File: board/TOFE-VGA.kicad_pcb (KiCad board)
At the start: 4 copper layers, 46 x 3 mm, 114 parts, among them P1 CONN_02X06, P601 3-RCA, U5V1 LP2985

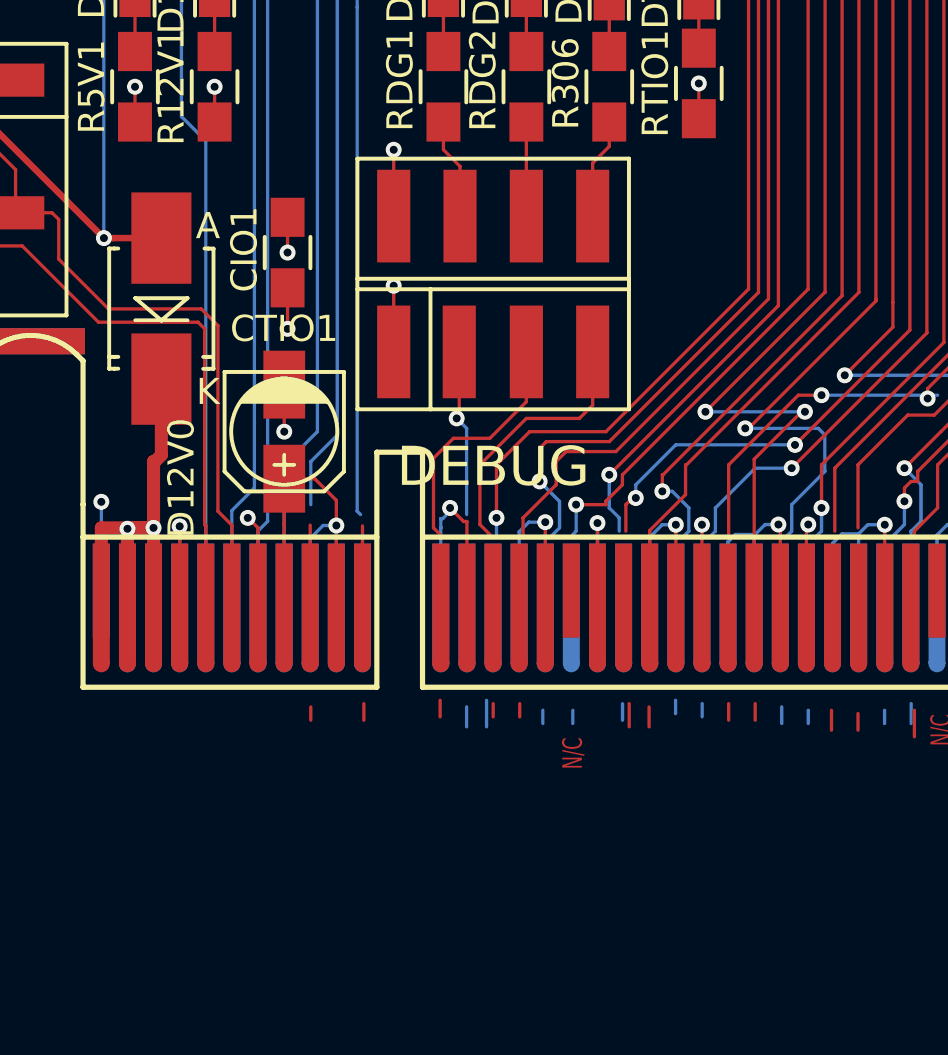
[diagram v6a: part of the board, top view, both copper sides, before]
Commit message: Updating PCB.
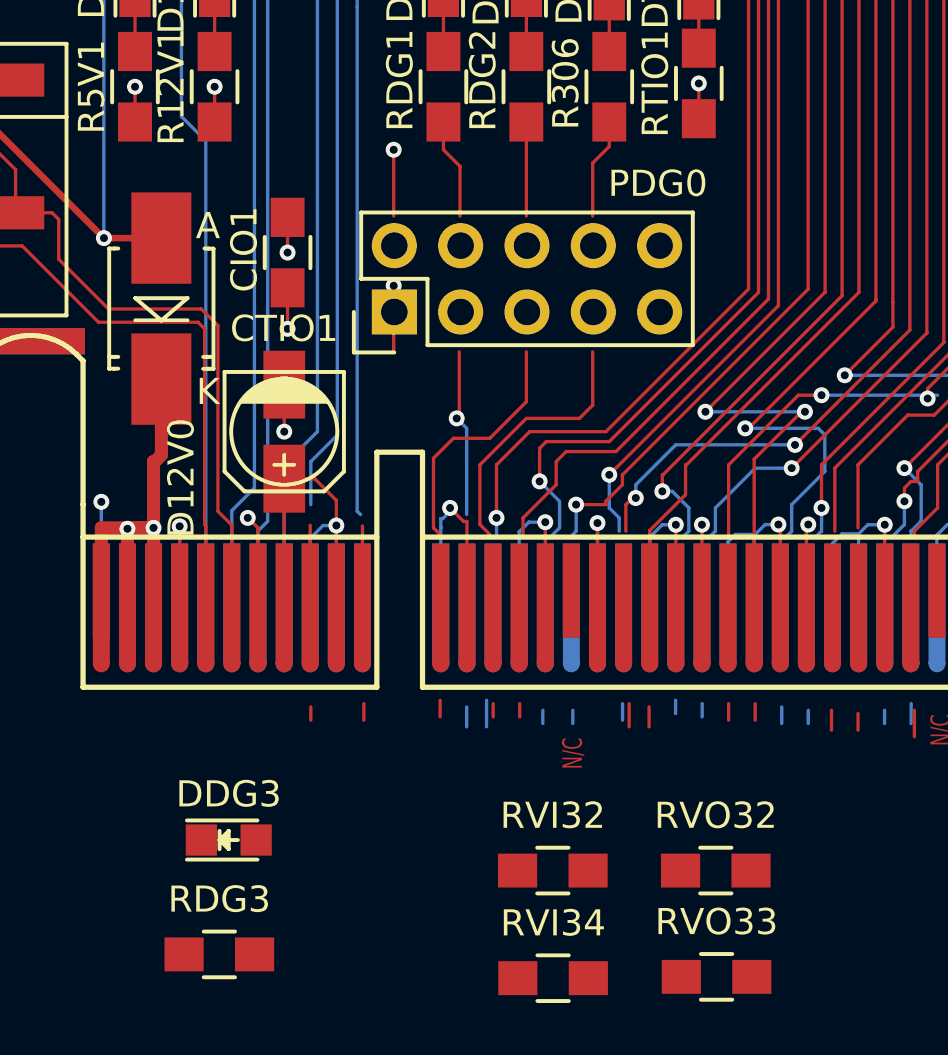
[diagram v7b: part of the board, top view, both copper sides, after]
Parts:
- added DDG3: LED, LEDs:LED_0805, F.Cu at (112.8, 164.3)
- added RDG3: 68R, Resistors_SMD:R_0805_HandSoldering, F.Cu at (112.4, 168.7)
- added RVI32: ?, Resistors_SMD:R_0805_HandSoldering, F.Cu at (125.2, 165.5)
- added RVI34: ?, Resistors_SMD:R_0805_HandSoldering, F.Cu at (125.2, 169.6)
- added RVO32: ?, Resistors_SMD:R_0805_HandSoldering, F.Cu at (131.4, 165.5)
- added RVO33: ?, Resistors_SMD:R_0805_HandSoldering, F.Cu at (131.5, 169.6)
- PDG0: footprint CON-SMD-2.54:TE-AMPMODU-MOD-II-4X2 -> Pin_Headers:Pin_Header_Straight_2x05
- moved PDG0 3.93 mm to (119.1, 144.1), turned to 90 degrees
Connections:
- PDG0 pad 3: Net-(PDG0-Pad3) -> /TOFE-VGA/TOFE/VGAIN_I2C_EN
- PDG0 pad 5: Net-(PDG0-Pad5) -> /TOFE-VGA/TOFE/VGAOUT_I2C_EN
- PDG0 pad 8: GND -> Net-(PDG0-Pad8)
- TOFE0 pad A13: Net-(PDG0-Pad3) -> /TOFE-VGA/TOFE/VGAIN_I2C_EN
- TOFE0 pad A14: Net-(PDG0-Pad5) -> /TOFE-VGA/TOFE/VGAOUT_I2C_EN
- TOFE0 pad A16: /TOFE-VGA/AD9984/FIELD -> Net-(PDG0-Pad7)
- TOFE0 pad A17: /TOFE-VGA/TOFE/VGAOUT_I2C_EN -> /TOFE-VGA/AD9984/FIELD
- TOFE0 pad A19: /TOFE-VGA/TOFE/VGAIN_I2C_EN -> /TOFE-VGA/AD9984/B5
- TOFE0 pad A33: /TOFE-VGA/AD9984/B5 -> Net-(TOFE0-PadA33)
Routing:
- net Net-(PDG0-Pad8): track 0.00 -> 60.8 mm, vias 0 -> 1
- net /TOFE-VGA/AD9984/VSOUT: track 41.4 -> 5.57 mm, vias 1 -> 0
- net /TOFE-VGA/AD9984/HSOUT: track 38.0 -> 7.00 mm, vias 1 -> 0
- net /TOFE-VGA/AD9984/SOGOUT: track 37.4 -> 7.14 mm
- net Net-(PDG0-Pad7): track 10.1 -> 40.2 mm
- net (no net): track 42.2 -> 53.7 mm, vias 1 -> 4
- net Net-(PDG0-Pad5): track 9.39 -> 0.00 mm
- net /TOFE-VGA/TOFE/VGAOUT_I2C_EN: track 97.5 -> 106.9 mm
- net Net-(PDG0-Pad3): track 6.43 -> 0.00 mm, vias 1 -> 0
- net Net-(PDG0-Pad6): track 3.60 -> 8.27 mm
- net Net-(P303-Pad8): track 0.94 -> 3.87 mm
- net +3V3: track 82.5 -> 79.9 mm, vias 26 -> 25
- net Net-(PDG0-Pad1): track 2.53 -> 0.00 mm, vias 1 -> 0
- net /TOFE-VGA/AD9984/R9: track 36.4 -> 35.2 mm
- net GND: track 179.1 -> 177.9 mm
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
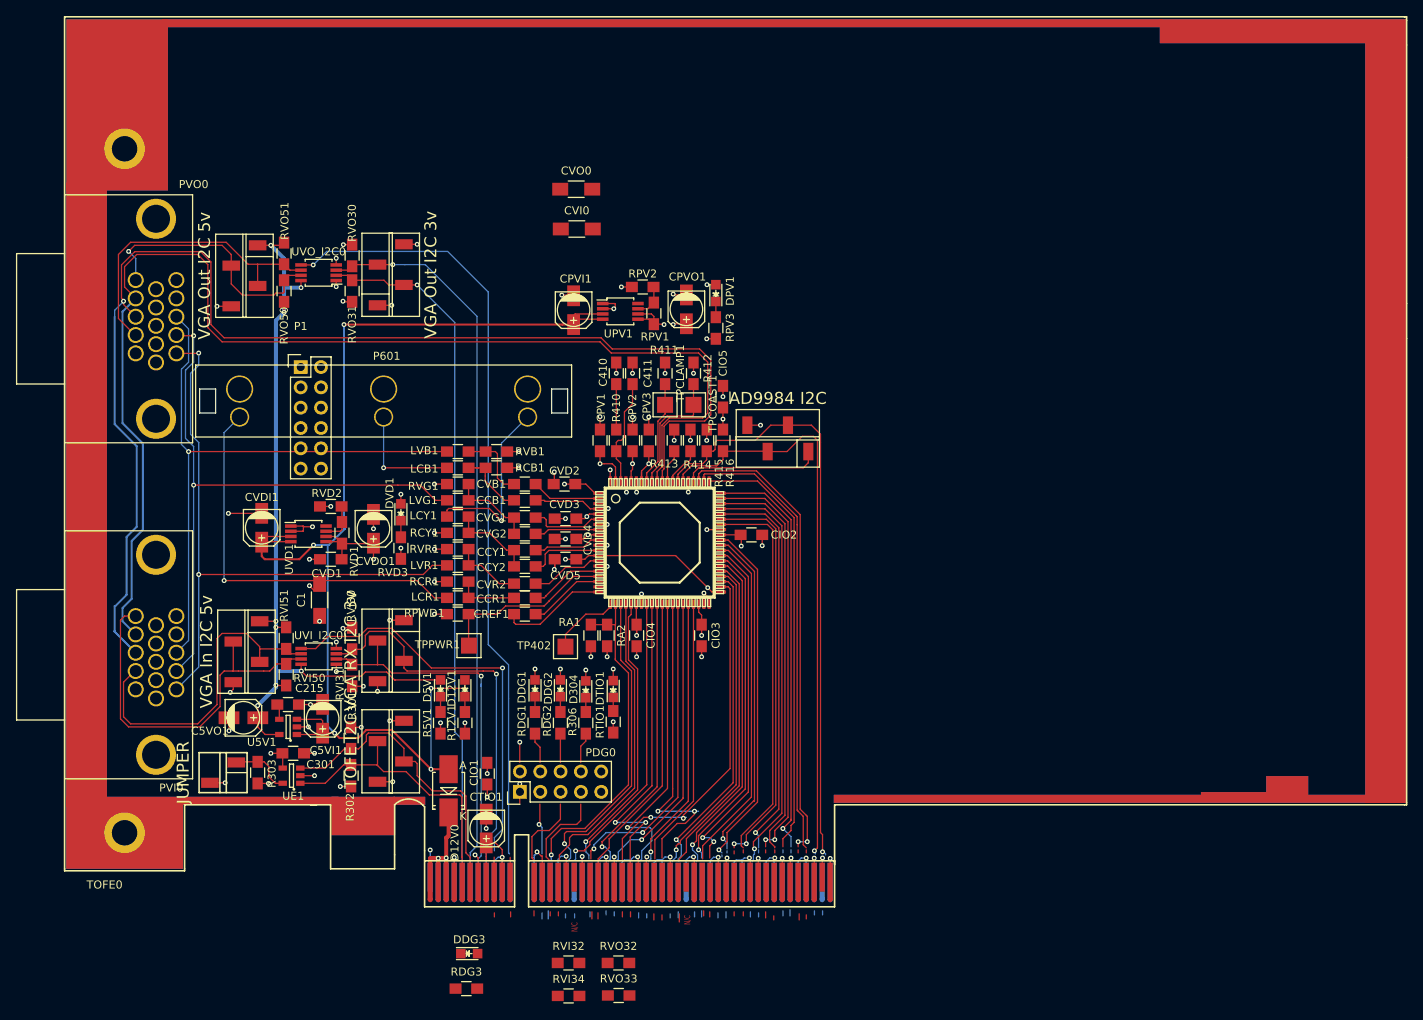
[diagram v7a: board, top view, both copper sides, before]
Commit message: Trying to import new netlist.
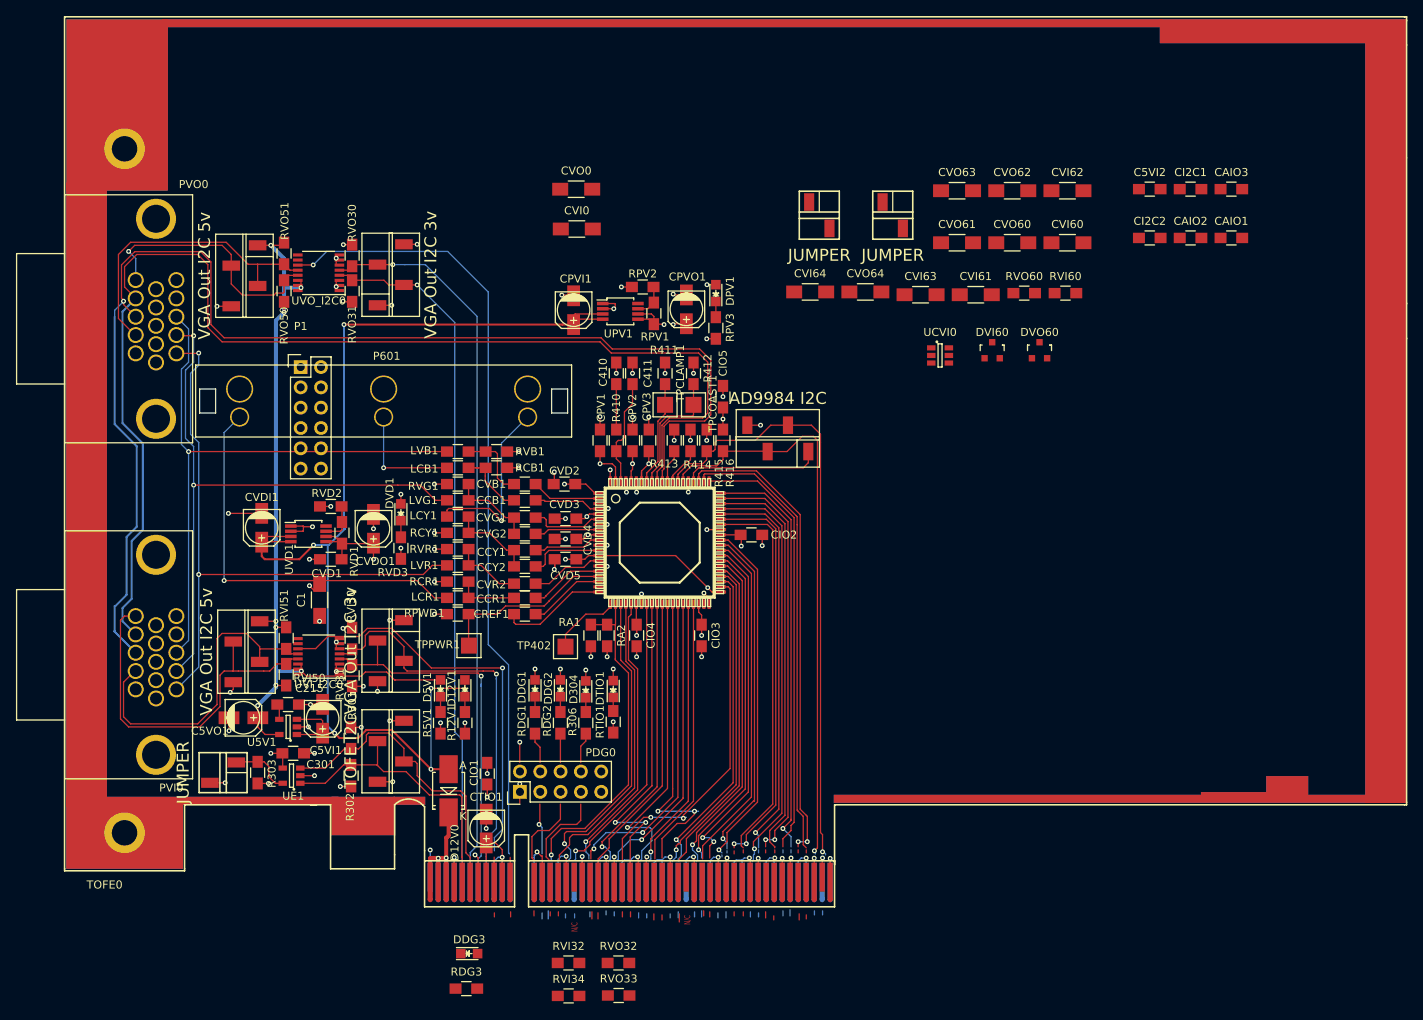
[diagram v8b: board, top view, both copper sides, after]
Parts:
- added C5VI2: 10n, Resistors_SMD:R_0805_HandSoldering, F.Cu at (197.8, 68.8)
- added CAIO1: 100n, Resistors_SMD:R_0805_HandSoldering, F.Cu at (208.0, 74.9)
- added CAIO2: 100n, Resistors_SMD:R_0805_HandSoldering, F.Cu at (202.9, 74.9)
- added CAIO3: 100n, Resistors_SMD:R_0805_HandSoldering, F.Cu at (208.0, 68.8)
- added CI2C1: 100n, Resistors_SMD:R_0805_HandSoldering, F.Cu at (202.9, 68.8)
- added CI2C2: 100n, Resistors_SMD:R_0805_HandSoldering, F.Cu at (197.8, 74.9)
- added CVI60: 100nF, Capacitors_SMD:C_1206_HandSoldering, F.Cu at (187.6, 75.5)
- added CVI61: 100nF, Capacitors_SMD:C_1206_HandSoldering, F.Cu at (176.1, 82.0)
- added CVI62: 100nF, Capacitors_SMD:C_1206_HandSoldering, F.Cu at (187.6, 69.0)
- added CVI63: 100nF, Capacitors_SMD:C_1206_HandSoldering, F.Cu at (169.2, 82.0)
- added CVI64: 100nF, Capacitors_SMD:C_1206_HandSoldering, F.Cu at (155.4, 81.6)
- added CVO60: 100nF, Capacitors_SMD:C_1206_HandSoldering, F.Cu at (180.7, 75.5)
- added CVO61: 100nF, Capacitors_SMD:C_1206_HandSoldering, F.Cu at (173.8, 75.5)
- added CVO62: 100nF, Capacitors_SMD:C_1206_HandSoldering, F.Cu at (180.7, 69.0)
- added CVO63: 100nF, Capacitors_SMD:C_1206_HandSoldering, F.Cu at (173.8, 69.0)
- added CVO64: 100nF, Capacitors_SMD:C_1206_HandSoldering, F.Cu at (162.3, 81.6)
- added DVI60: BAT54C, TO_SOT_Packages_SMD:SOT-23, F.Cu at (178.1, 88.9)
- added DVO60: BAT54C, TO_SOT_Packages_SMD:SOT-23, F.Cu at (184.1, 88.9)
- added JVI60: JUMPER, CON-SMD-2.54:HARWIN-M20-87-2x1, F.Cu at (165.7, 72.1)
- added JVO60: JUMPER, CON-SMD-2.54:HARWIN-M20-87-2x1, F.Cu at (156.5, 72.1)
- added RVI60: 2K2, Resistors_SMD:R_0805_HandSoldering, F.Cu at (187.3, 81.8)
- added RVO60: 2K2, Resistors_SMD:R_0805_HandSoldering, F.Cu at (182.2, 81.8)
- added UCVI0: SP724AH, TO_SOT_Packages_SMD:SOT-23-6, F.Cu at (171.6, 89.6)
- C5VO1: value 2u2 -> 22u
- PVI_I2C3: value VGA RX I2C 3v -> VGA Out I2C 3v
- PVI_I2C5: value VGA In I2C 5v -> VGA Out I2C 5v
- UVI_I2C0, UVO_I2C0: value TCA9617A -> TPD7S019; footprint Housings_SSOP:MSOP-8_3x3mm_Pitch0.65mm -> Housings_SSOP:SSOP-16_3.9x4.9mm_Pitch0.635mm
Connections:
- P1 pad 10: /TOFE-VGA/VGA/VGAOUT_B -> /TOFE-VGA/VGA/VGAIN_B
- P1 pad 6: /TOFE-VGA/VGA/VGAOUT_R -> /TOFE-VGA/VGA/VGAIN_R
- P1 pad 8: /TOFE-VGA/VGA/VGAOUT_G -> /TOFE-VGA/VGA/VGAIN_G
- PVI0 pad 12: /TOFE-VGA/VGA/VGAIN5V_SDA -> /TOFE-VGA/VGA/VGAOUT5V_SDA
- PVI0 pad 13: /TOFE-VGA/VGA/VGAIN_HSYNC -> /TOFE-VGA/VGA/VGAOUT_HSYNC
- PVI0 pad 14: /TOFE-VGA/VGA/VGAIN_VSYNC -> /TOFE-VGA/VGA/VGAOUT_VSYNC
- PVI0 pad 15: /TOFE-VGA/VGA/VGAIN5V_SCL -> /TOFE-VGA/VGA/VGAOUT5V_SCL
- PVI_I2C5 pad 2: /TOFE-VGA/VGA/VGAIN5V_SCL -> /TOFE-VGA/VGA/VGAOUT5V_SCL
- PVI_I2C5 pad 3: /TOFE-VGA/VGA/VGAIN5V_SDA -> /TOFE-VGA/VGA/VGAOUT5V_SDA
- PVO0 pad 1: /TOFE-VGA/VGA/VGAOUT_R -> /TOFE-VGA/VGA/VGAIN_R
- PVO0 pad 2: /TOFE-VGA/VGA/VGAOUT_G -> /TOFE-VGA/VGA/VGAIN_G
- PVO0 pad 3: /TOFE-VGA/VGA/VGAOUT_B -> /TOFE-VGA/VGA/VGAIN_B
- RVI50 pad 2: /TOFE-VGA/VGA/VGAIN5V_SCL -> /TOFE-VGA/VGA/VGAOUT5V_SCL
- RVI51 pad 2: /TOFE-VGA/VGA/VGAIN5V_SDA -> /TOFE-VGA/VGA/VGAOUT5V_SDA
- TOFE0 pad A13: /TOFE-VGA/TOFE/VGAIN_I2C_EN -> /TOFE-VGA/AD9984/VSOUT
- TOFE0 pad A14: /TOFE-VGA/TOFE/VGAOUT_I2C_EN -> /TOFE-VGA/AD9984/HSOUT
- TOFE0 pad A16: Net-(PDG0-Pad7) -> /TOFE-VGA/AD9984/R8
- TOFE0 pad A17: /TOFE-VGA/AD9984/FIELD -> /TOFE-VGA/AD9984/R7
- TOFE0 pad A19: /TOFE-VGA/AD9984/B5 -> /TOFE-VGA/AD9984/R6
- TOFE0 pad A21: /TOFE-VGA/AD9984/SDA_AD9984 -> /TOFE-VGA/AD9984/R3
- TOFE0 pad A22: /TOFE-VGA/AD9984/SCL_AD9984 -> /TOFE-VGA/AD9984/R2
- TOFE0 pad A25: /TOFE-VGA/AD9984/B0 -> /TOFE-VGA/AD9984/G9
- TOFE0 pad A26: /TOFE-VGA/AD9984/B1 -> /TOFE-VGA/AD9984/G8
- TOFE0 pad A29: /TOFE-VGA/AD9984/B2 -> /TOFE-VGA/AD9984/DATACK
- TOFE0 pad A30: /TOFE-VGA/AD9984/B3 -> /TOFE-VGA/AD9984/SOGOUT
- TOFE0 pad A32: /TOFE-VGA/AD9984/B4 -> /TOFE-VGA/AD9984/G4
- TOFE0 pad A35: /TOFE-VGA/AD9984/B6 -> /TOFE-VGA/AD9984/G1
- TOFE0 pad A36: /TOFE-VGA/AD9984/B7 -> /TOFE-VGA/AD9984/G0
- TOFE0 pad A39: /TOFE-VGA/AD9984/B8 -> /TOFE-VGA/AD9984/B7
- TOFE0 pad A40: /TOFE-VGA/AD9984/B9 -> /TOFE-VGA/AD9984/B6
- TOFE0 pad A43: /TOFE-VGA/AD9984/G0 -> /TOFE-VGA/AD9984/B3
- TOFE0 pad A44: /TOFE-VGA/AD9984/G1 -> /TOFE-VGA/AD9984/B2
- TOFE0 pad A47: /TOFE-VGA/AD9984/G2 -> /TOFE-VGA/AD9984/SDA_AD9984
- TOFE0 pad A48: /TOFE-VGA/AD9984/G3 -> /TOFE-VGA/AD9984/SCL_AD9984
- TOFE0 pad A5: /TOFE-VGA/TOFE/VGAOUT_SCL -> /TOFE-VGA/VGA/VGAOUT_SCL
- TOFE0 pad A6: /TOFE-VGA/VGA/VGAOUT_SCL -> /TOFE-VGA/TOFE/VGAOUT_SCL
- TOFE0 pad A7: /TOFE-VGA/TOFE/VGAIN_SCL -> /TOFE-VGA/VGA/VGAIN_SCL
- TOFE0 pad A8: /TOFE-VGA/VGA/VGAIN_SCL -> /TOFE-VGA/TOFE/VGAIN_SCL
- TOFE0 pad B11: /TOFE-VGA/AD9984/R1 -> /TOFE-VGA/TOFE/VGAOUT_I2C_EN
- TOFE0 pad B12: /TOFE-VGA/AD9984/R2 -> Net-(PDG0-Pad7)
- TOFE0 pad B14: /TOFE-VGA/AD9984/R3 -> /TOFE-VGA/AD9984/FIELD
- TOFE0 pad B15: /TOFE-VGA/AD9984/R4 -> /TOFE-VGA/AD9984/R9
- TOFE0 pad B20: /TOFE-VGA/AD9984/R6 -> /TOFE-VGA/AD9984/R4
- TOFE0 pad B23: /TOFE-VGA/AD9984/R7 -> /TOFE-VGA/AD9984/R1
- TOFE0 pad B24: /TOFE-VGA/AD9984/R8 -> /TOFE-VGA/AD9984/R0
- TOFE0 pad B27: /TOFE-VGA/AD9984/DATACK -> /TOFE-VGA/AD9984/G7
- TOFE0 pad B28: /TOFE-VGA/AD9984/SOGOUT -> /TOFE-VGA/AD9984/G6
- TOFE0 pad B30: /TOFE-VGA/AD9984/R9 -> /TOFE-VGA/AD9984/G5
- TOFE0 pad B33: /TOFE-VGA/AD9984/G9 -> /TOFE-VGA/AD9984/G3
- TOFE0 pad B34: /TOFE-VGA/AD9984/G8 -> /TOFE-VGA/AD9984/G2
- TOFE0 pad B37: /TOFE-VGA/AD9984/G7 -> /TOFE-VGA/AD9984/B9
- TOFE0 pad B38: /TOFE-VGA/AD9984/G6 -> /TOFE-VGA/AD9984/B8
- TOFE0 pad B41: /TOFE-VGA/AD9984/G5 -> /TOFE-VGA/AD9984/B5
- TOFE0 pad B42: /TOFE-VGA/AD9984/G4 -> /TOFE-VGA/AD9984/B4
- TOFE0 pad B45: /TOFE-VGA/AD9984/HSOUT -> /TOFE-VGA/AD9984/B1
- TOFE0 pad B46: /TOFE-VGA/AD9984/VSOUT -> /TOFE-VGA/AD9984/B0
- TOFE0 pad B9: /TOFE-VGA/AD9984/R0 -> /TOFE-VGA/TOFE/VGAIN_I2C_EN
- U5V1 pad 4: Net-(C215-Pad1) -> Net-(C5VI2-Pad1)
- UVI_I2C0 pad 1: +3V3 -> +5V
- UVI_I2C0 pad 2: /TOFE-VGA/VGA/VGAIN_SCL -> +5V
- UVI_I2C0 pad 3: /TOFE-VGA/TOFE/VGAIN_SCL -> /TOFE-VGA/VGA/VGAIN_B
- UVI_I2C0 pad 4: GND -> /TOFE-VGA/VGA/VGAIN_G
- UVI_I2C0 pad 5: /TOFE-VGA/TOFE/VGAIN_I2C_EN -> /TOFE-VGA/VGA/VGAIN_R
- UVI_I2C0 pad 6: /TOFE-VGA/VGA/VGAIN5V_SDA -> GND
- UVI_I2C0 pad 7: /TOFE-VGA/VGA/VGAIN5V_SCL -> +3V3
- UVI_I2C0 pad 8: +5V -> Net-(CVI63-Pad1)
- UVO_I2C0 pad 1: +3V3 -> +5V
- UVO_I2C0 pad 2: /TOFE-VGA/VGA/VGAOUT_SCL -> +5V
- UVO_I2C0 pad 3: /TOFE-VGA/TOFE/VGAOUT_SCL -> /TOFE-VGA/VGA/VGAIN_B
- UVO_I2C0 pad 4: GND -> /TOFE-VGA/VGA/VGAIN_G
- UVO_I2C0 pad 5: /TOFE-VGA/TOFE/VGAOUT_I2C_EN -> /TOFE-VGA/VGA/VGAIN_R
- UVO_I2C0 pad 6: /TOFE-VGA/VGA/VGAOUT5V_SDA -> GND
- UVO_I2C0 pad 7: /TOFE-VGA/VGA/VGAOUT5V_SCL -> +3V3
- UVO_I2C0 pad 8: +5V -> Net-(CVO63-Pad1)
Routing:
- net /TOFE-VGA/TOFE/VGAOUT_I2C_EN: track 106.9 -> 2.98 mm, vias 1 -> 0
- net /TOFE-VGA/VGA/VGAOUT_SCL: track 14.2 -> 86.1 mm, vias 0 -> 1
- net Net-(PDG0-Pad8): track 60.8 -> 0.00 mm, vias 1 -> 0
- net /TOFE-VGA/TOFE/VGAIN_I2C_EN: track 51.6 -> 3.01 mm, vias 1 -> 0
- net /TOFE-VGA/VGA/VGAOUT5V_SCL: track 32.4 -> 79.4 mm
- net /TOFE-VGA/VGA/VGAIN5V_SCL: track 46.9 -> 0.00 mm
- net /TOFE-VGA/VGA/VGAOUT_HSYNC: track 4.69 -> 51.0 mm
- net /TOFE-VGA/VGA/VGAIN_HSYNC: track 155.2 -> 108.9 mm
- net /TOFE-VGA/VGA/VGAIN5V_SDA: track 41.4 -> 0.00 mm
- net /TOFE-VGA/VGA/VGAOUT5V_SDA: track 38.6 -> 80.0 mm
- net Net-(PDG0-Pad7): track 40.2 -> 0.00 mm
- net /TOFE-VGA/AD9984/VSOUT: track 5.57 -> 41.4 mm, vias 0 -> 1
- net /TOFE-VGA/AD9984/HSOUT: track 7.00 -> 38.0 mm, vias 0 -> 1
- net /TOFE-VGA/AD9984/SOGOUT: track 7.14 -> 37.4 mm
- net /TOFE-VGA/TOFE/VGAIN_SCL: track 73.0 -> 102.4 mm
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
